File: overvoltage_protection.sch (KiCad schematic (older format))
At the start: 6 parts

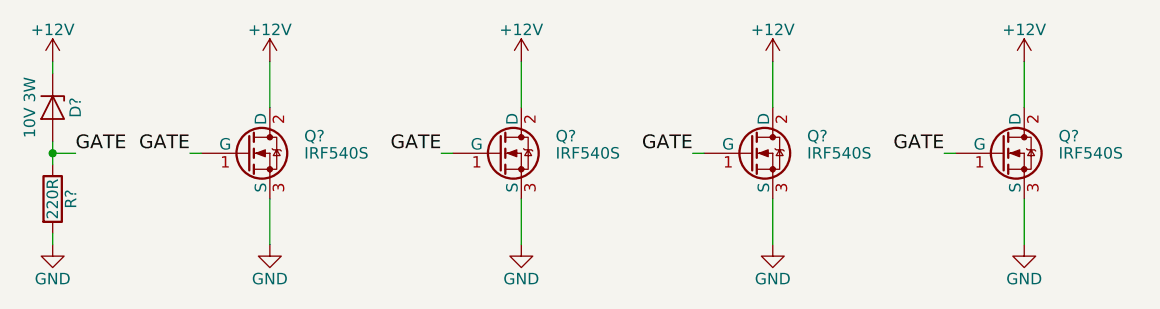
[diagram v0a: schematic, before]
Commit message: add MPN and change footprints
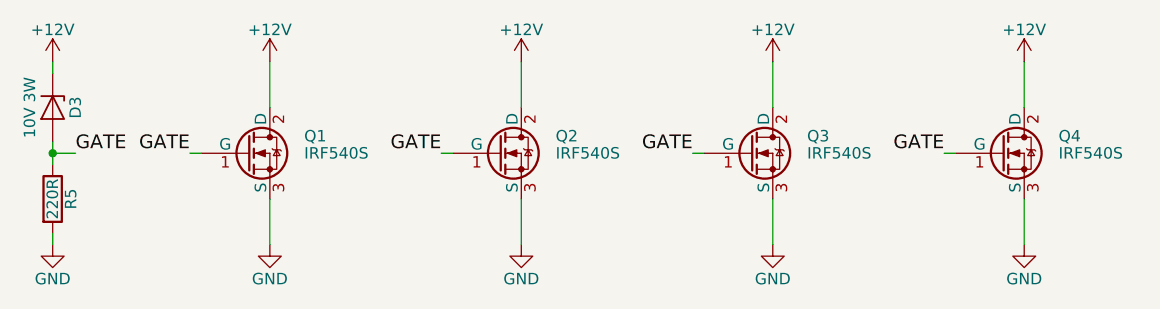
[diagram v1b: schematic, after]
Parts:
- gave numbers to parts that had none: 6
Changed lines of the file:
@@
 LIBS:contrib
 LIBS:valves
+LIBS:MB_DEVICE
 LIBS:power_board-cache
 EELAYER 25 0
@@
 $EndDescr
 $Comp
-L D_Zener D?
+L D_Zener D3
 U 1 1 5AA80EAB
 P 4500 3600
-F 0 "D?" H 4500 3700 50  0000 C CNN
+F 0 "D3" H 4500 3700 50  0000 C CNN
 F 1 "10V 3W" H 4500 3500 50  0000 C CNN
 F 2 "Diodes_SMD:D_SMB" H 4500 3600 50  0001 C CNN
@@
 $EndComp
 $Comp
-L +12V #PWR?
+L +12V #PWR057
 U 1 1 5AA812B6
 P 5450 3400
-F 0 "#PWR?" H 5450 3250 50  0001 C CNN
+F 0 "#PWR057" H 5450 3250 50  0001 C CNN
 F 1 "+12V" H 5450 3540 50  0000 C CNN
 F 2 "" H 5450 3400 50  0001 C CNN
@@
 $EndComp
 $Comp
-L IRF540N Q?
+L IRF540N Q1
 U 1 1 5AA81315
 P 5350 3800
-F 0 "Q?" H 5600 3875 50  0000 L CNN
+F 0 "Q1" H 5600 3875 50  0000 L CNN
 F 1 "IRF540S" H 5600 3800 50  0000 L CNN
 F 2 "TO_SOT_Packages_SMD:TO-263-2" H 5600 3725 50  0001 L CIN
@@
 	5450 3400 5450 3600
 $Comp
-L +12V #PWR?
+L +12V #PWR058
 U 1 1 5AA8139B
 P 4500 3400
-F 0 "#PWR?" H 4500 3250 50  0001 C CNN
+F 0 "#PWR058" H 4500 3250 50  0001 C CNN
 F 1 "+12V" H 4500 3540 50  0000 C CNN
 F 2 "" H 4500 3400 50  0001 C CNN
@@
 	4500 3400 4500 3450
 $Comp
-L R R?
+L R R5
 U 1 1 5AA8146E
 P 4500 4000
-F 0 "R?" V 4580 4000 50  0000 C CNN
+F 0 "R5" V 4580 4000 50  0000 C CNN
 F 1 "220R" V 4500 4000 50  0000 C CNN
 F 2 "Resistors_SMD:R_1206" V 4430 4000 50  0001 C CNN
@@
 $EndComp
 $Comp
-L GND #PWR?
+L GND #PWR059
 U 1 1 5AA814B6
 P 5450 4200
-F 0 "#PWR?" H 5450 3950 50  0001 C CNN
+F 0 "#PWR059" H 5450 3950 50  0001 C CNN
 F 1 "GND" H 5450 4050 50  0000 C CNN
 F 2 "" H 5450 4200 50  0001 C CNN
@@
 $EndComp
 $Comp
-L GND #PWR?
+L GND #PWR060
 U 1 1 5AA814D1
 P 4500 4200
-F 0 "#PWR?" H 4500 3950 50  0001 C CNN
+F 0 "#PWR060" H 4500 3950 50  0001 C CNN
 F 1 "GND" H 4500 4050 50  0000 C CNN
 F 2 "" H 4500 4200 50  0001 C CNN
@@
 	5100 3800 5150 3800
 $Comp
-L +12V #PWR?
+L +12V #PWR061
 U 1 1 5AA81A7B
 P 6550 3400
-F 0 "#PWR?" H 6550 3250 50  0001 C CNN
+F 0 "#PWR061" H 6550 3250 50  0001 C CNN
 F 1 "+12V" H 6550 3540 50  0000 C CNN
 F 2 "" H 6550 3400 50  0001 C CNN
@@
 $EndComp
 $Comp
-L IRF540N Q?
+L IRF540N Q2
 U 1 1 5AA81A82
 P 6450 3800
-F 0 "Q?" H 6700 3875 50  0000 L CNN
+F 0 "Q2" H 6700 3875 50  0000 L CNN
 F 1 "IRF540S" H 6700 3800 50  0000 L CNN
 F 2 "TO_SOT_Packages_SMD:TO-263-2" H 6700 3725 50  0001 L CIN
@@
 	6550 3400 6550 3600
 $Comp
-L GND #PWR?
+L GND #PWR062
 U 1 1 5AA81A89
 P 6550 4200
-F 0 "#PWR?" H 6550 3950 50  0001 C CNN
+F 0 "#PWR062" H 6550 3950 50  0001 C CNN
 F 1 "GND" H 6550 4050 50  0000 C CNN
 F 2 "" H 6550 4200 50  0001 C CNN
@@
 	6200 3800 6250 3800
 $Comp
-L +12V #PWR?
+L +12V #PWR063
 U 1 1 5AA81BB1
 P 7650 3400
-F 0 "#PWR?" H 7650 3250 50  0001 C CNN
+F 0 "#PWR063" H 7650 3250 50  0001 C CNN
 F 1 "+12V" H 7650 3540 50  0000 C CNN
 F 2 "" H 7650 3400 50  0001 C CNN
@@
 $EndComp
 $Comp
-L IRF540N Q?
+L IRF540N Q3
 U 1 1 5AA81BB8
 P 7550 3800
-F 0 "Q?" H 7800 3875 50  0000 L CNN
+F 0 "Q3" H 7800 3875 50  0000 L CNN
 F 1 "IRF540S" H 7800 3800 50  0000 L CNN
 F 2 "TO_SOT_Packages_SMD:TO-263-2" H 7800 3725 50  0001 L CIN
@@
 	7650 3400 7650 3600
 $Comp
-L GND #PWR?
+L GND #PWR064
 U 1 1 5AA81BBF
 P 7650 4200
-F 0 "#PWR?" H 7650 3950 50  0001 C CNN
+F 0 "#PWR064" H 7650 3950 50  0001 C CNN
 F 1 "GND" H 7650 4050 50  0000 C CNN
 F 2 "" H 7650 4200 50  0001 C CNN
@@
 	7300 3800 7350 3800
 $Comp
-L +12V #PWR?
+L +12V #PWR065
 U 1 1 5AA81BE5
 P 8750 3400
-F 0 "#PWR?" H 8750 3250 50  0001 C CNN
+F 0 "#PWR065" H 8750 3250 50  0001 C CNN
 F 1 "+12V" H 8750 3540 50  0000 C CNN
 F 2 "" H 8750 3400 50  0001 C CNN
@@
 $EndComp
 $Comp
-L IRF540N Q?
+L IRF540N Q4
 U 1 1 5AA81BEC
 P 8650 3800
-F 0 "Q?" H 8900 3875 50  0000 L CNN
+F 0 "Q4" H 8900 3875 50  0000 L CNN
 F 1 "IRF540S" H 8900 3800 50  0000 L CNN
 F 2 "TO_SOT_Packages_SMD:TO-263-2" H 8900 3725 50  0001 L CIN
@@
 	8750 3400 8750 3600
 $Comp
-L GND #PWR?
+L GND #PWR066
 U 1 1 5AA81BF3
 P 8750 4200
-F 0 "#PWR?" H 8750 3950 50  0001 C CNN
+F 0 "#PWR066" H 8750 3950 50  0001 C CNN
 F 1 "GND" H 8750 4050 50  0000 C CNN
 F 2 "" H 8750 4200 50  0001 C CNN

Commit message: kicost file added
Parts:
- R5: MPN (none) -> RR1220P-103-D
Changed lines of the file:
@@
 LIBS:contrib
 LIBS:valves
-LIBS:MB_DEVICE
 LIBS:power_board-cache
 EELAYER 25 0
@@
 F 2 "Resistors_SMD:R_1206" V 4430 4000 50  0001 C CNN
 F 3 "" H 4500 4000 50  0001 C CNN
+F 4 "RR1220P-103-D " V 4500 4000 60  0001 C CNN "MPN"
 	1    4500 4000
 	1    0    0    -1
